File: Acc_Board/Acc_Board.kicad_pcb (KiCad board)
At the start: 2 copper layers, 139.7 x 88.9 mm, 84 parts, among them J1 AIRs Power, J10 Conn_01x02_Pin, J12 776087-1, J2 IsoSPI, J3 IMD BAT, J4 HV Power, J5 HVIL, J6 IMD, J7 Current Sensor, J8 Fans, J9 Shutdown IL, K1 Relay_SPST-NO, K2 Latching Relay, Q1 STS6NF20V, Q2 STS6NF20V, Q3 STS6NF20V, Q4 STS6NF20V, U1 ISO1050DUB, U10 DK1A1B-12V, U11 NSL-32, U12 LTC6820, U13 NAND, U15 MCP6004, U16 NSL-32, U17 NSL-32, U2 NUCLEO-L432KC, U3 LM555N, U4 PQDE6W-Q110-S5-H-D, U5 R-78B5.0-2.0, U6 NSL-32, U7 DK1A1B-12V, U8 LM7809_TO220, U9 NSL-32

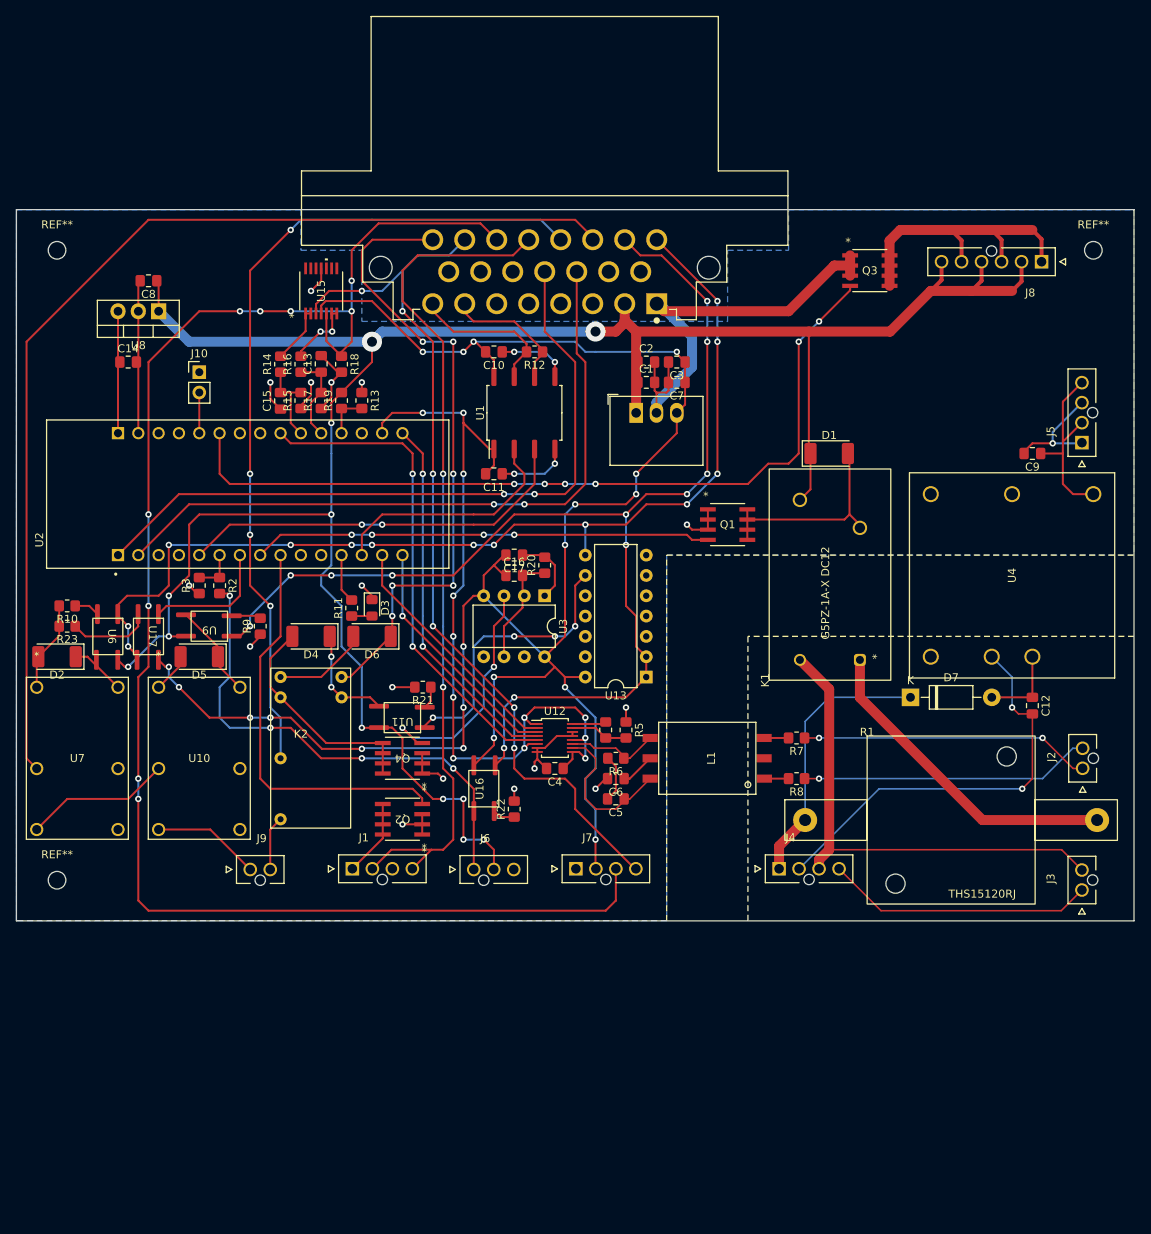
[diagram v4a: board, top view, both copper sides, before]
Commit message: acc board silkscreen done
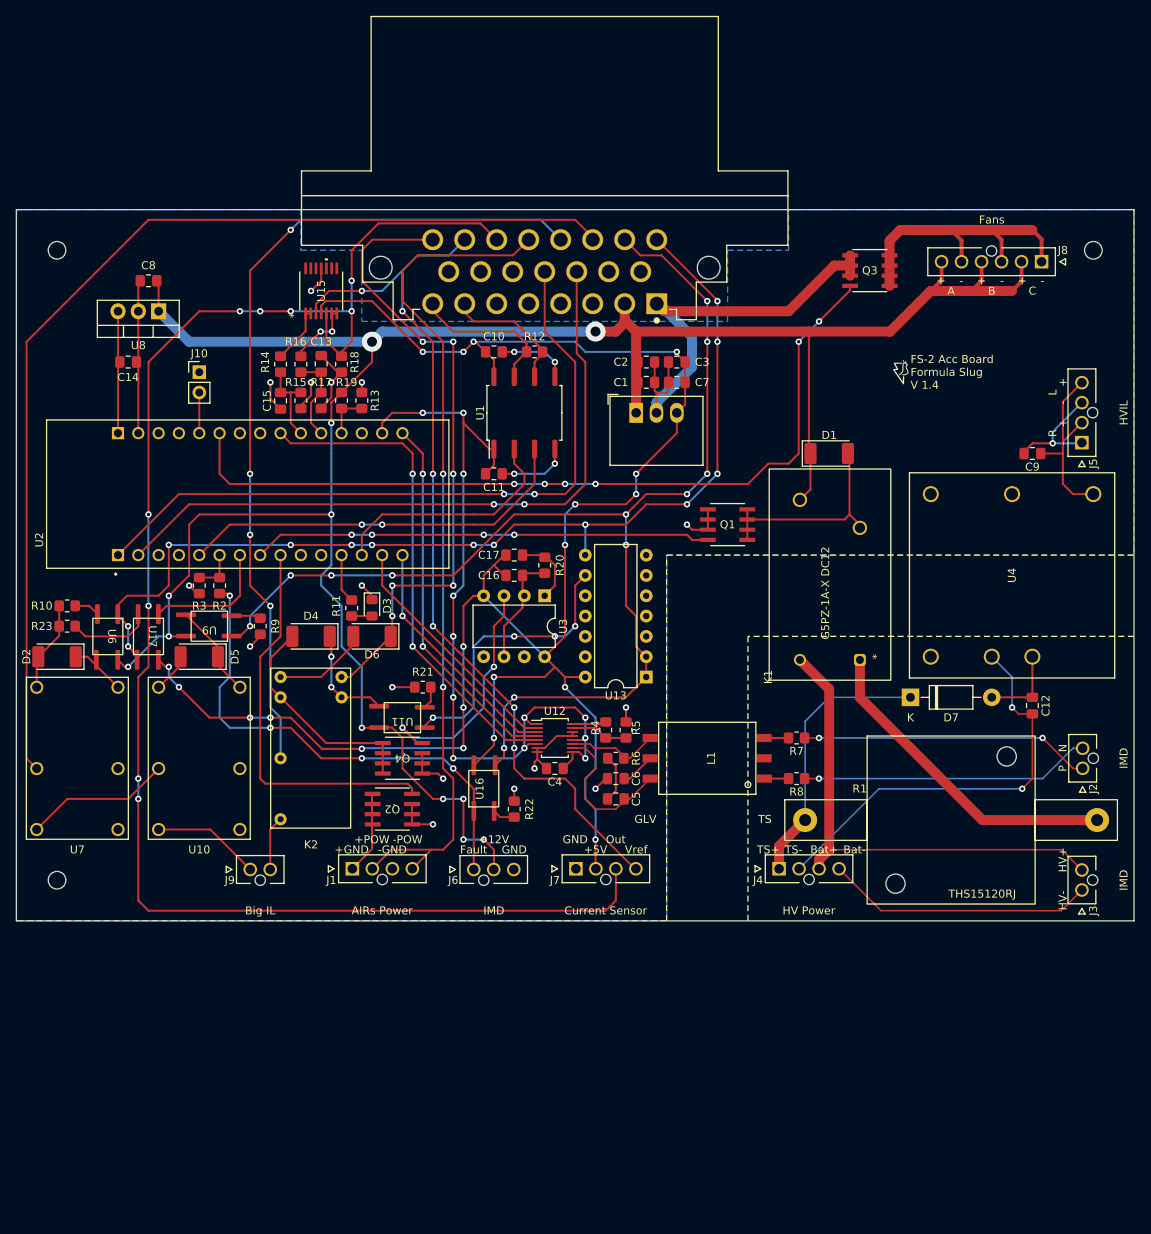
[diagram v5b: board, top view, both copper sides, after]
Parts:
- added G***: LOGO, 1FS_2_Global_Footprint_Library:FORMULA SLUG, F.Cu at (126.4, 33.1)
- moved Q2 1.80 mm to (59.7, 87.6)
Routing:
- net /Precharge_Control: track 51.0 -> 49.2 mm
- net /AIRS+_GND: track 9.67 -> 10.5 mm
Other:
- board text added: "+"
- board text added: "+12V"
- board text added: "+5V"
- board text added: "+GND"
- board text added: "+POW"
- board text added: "-"
- board text added: "-GND"
- board text added: "-POW"
- board text added: "A"
- board text added: "AIRs Power"
- board text added: "B"
- board text added: "Bat+"
- board text added: "Bat-"
- board text added: "Big IL"
- board text added: "C"
- board text added: "Current Sensor"
- board text added: "FS-2 Acc Board Formula Slug V 1.4"
- board text added: "Fans"
- board text added: "Fault"
- board text added: "GLV"
- board text added: "GND"
- board text added: "HV Power"
- board text added: "HV+"
- board text added: "HV-"
- board text added: "HVIL"
- board text added: "IMD"
- board text added: "L"
- board text added: "N"
- board text added: "Out"
- board text added: "P"
- board text added: "R"
- board text added: "TS"
- board text added: "TS+"
- board text added: "TS-"
- board text added: "Vref"

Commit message: Fixed sharp angle traces on acc board
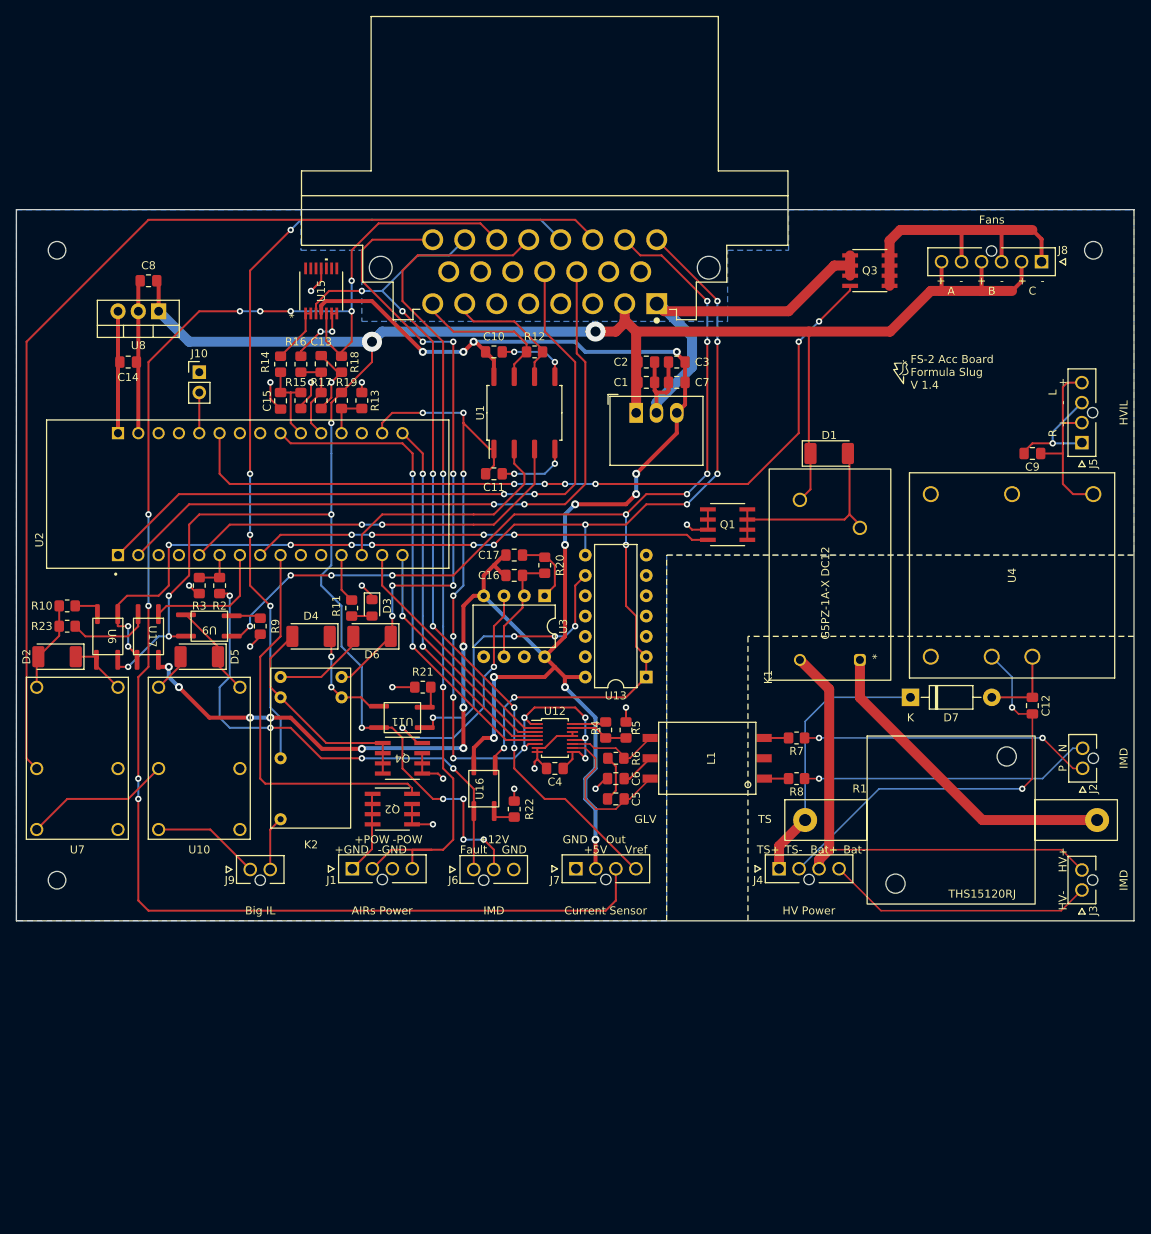
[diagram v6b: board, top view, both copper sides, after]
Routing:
- net /Current_Vref: track 113.0 -> 110.0 mm
- net /BMS_FAULT_5V: track 128.0 -> 129.5 mm
- net /Fan_Control: track 103.2 -> 101.7 mm
- net +12V: track 289.9 -> 288.5 mm
- net /AIRS+_12V: track 106.1 -> 107.5 mm
- net +5V: track 240.9 -> 242.2 mm
- net Net-(J8-Pad1): track 37.5 -> 36.5 mm
- net Net-(D2-K): track 6.87 -> 7.75 mm

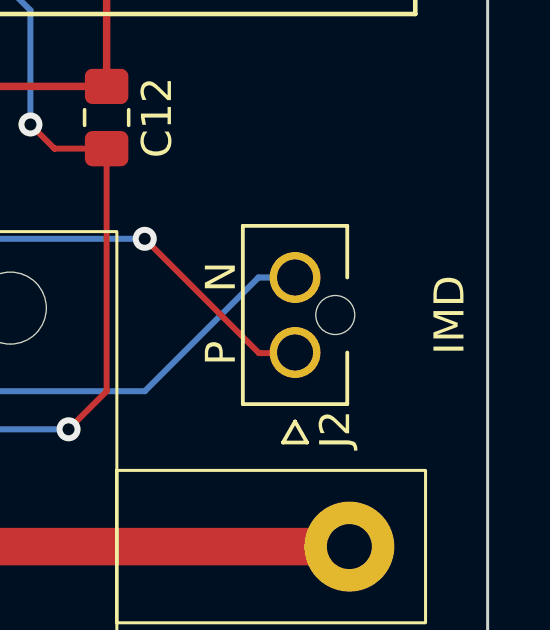
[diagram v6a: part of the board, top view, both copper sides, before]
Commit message: fixed minor silkscreen issue
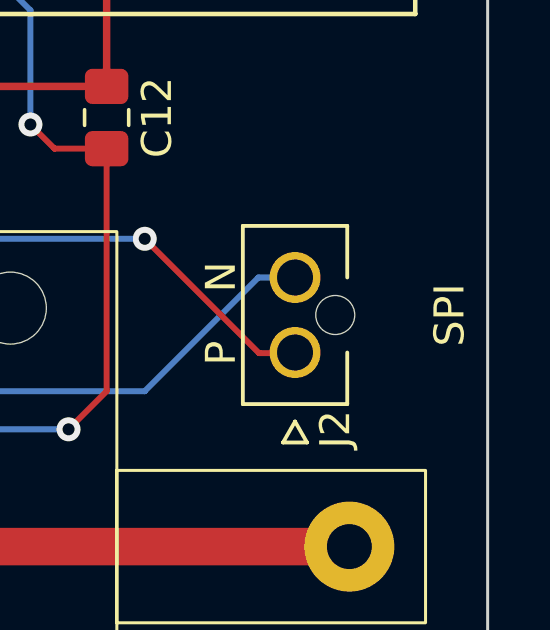
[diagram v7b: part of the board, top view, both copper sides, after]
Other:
- board text added: "SPI"
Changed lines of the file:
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@@
     (effects (font (size 1 1) (thickness 0.15)))
   )
-  (gr_text "IMD" (at 151.13 81.28 90) (layer "F.SilkS")
+  (gr_text "SPI" (at 151.13 81.28 90) (layer "F.SilkS")
     (effects (font (size 1 1) (thickness 0.15)))
   )

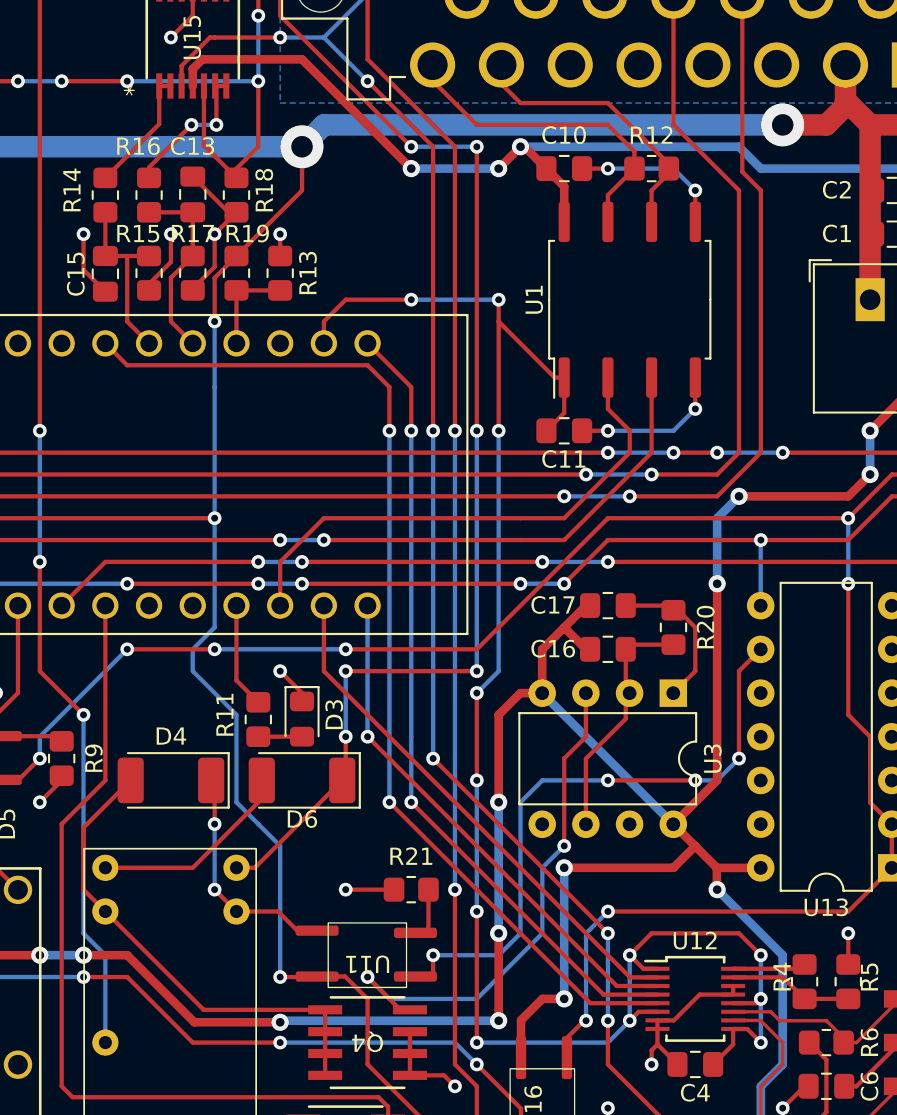
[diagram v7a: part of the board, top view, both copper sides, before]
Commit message: acc board minor fixes to trace isolation
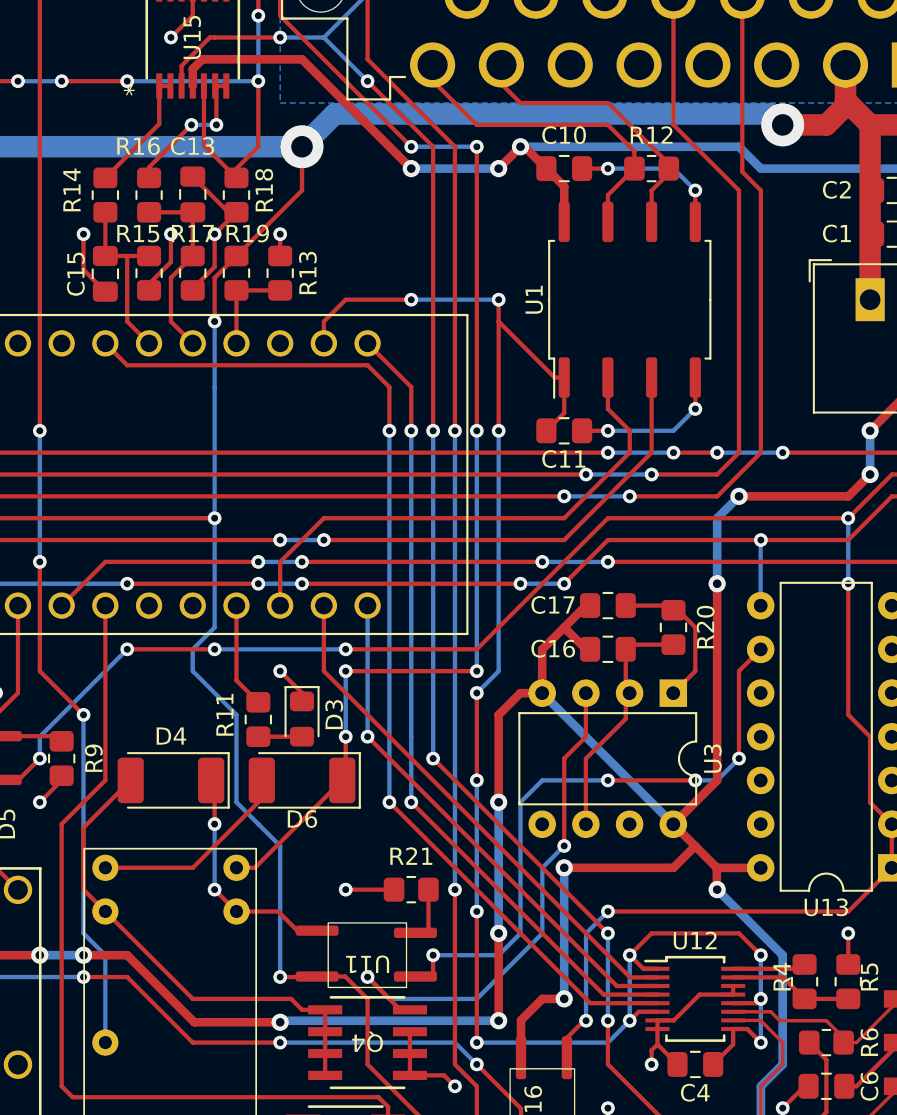
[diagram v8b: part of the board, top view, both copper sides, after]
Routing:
- net +12V: track 288.5 -> 289.0 mm
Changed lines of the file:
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@@
   (via (at 68.58 91.44) (size 0.8) (drill 0.4) (layers "F.Cu" "B.Cu") (net 1))
   (via (at 55.88 77.47) (size 0.8) (drill 0.4) (layers "F.Cu" "B.Cu") (net 1))
-  (segment (start 58.42 27.94) (end 57.15 29.21) (width 1.25) (layer "B.Cu") (net 1))
+  (segment (start 84.455 27.305) (end 59.055 27.305) (width 1.25) (layer "B.Cu") (net 1))
   (segment (start 50.8 59.69) (end 53.34 62.23) (width 0.25) (layer "B.Cu") (net 1))
   (segment (start 53.34 62.23) (end 53.34 67.31) (width 0.25) (layer "B.Cu") (net 1))
@@
   (segment (start 50.8 58.42) (end 50.8 59.69) (width 0.25) (layer "B.Cu") (net 1))
   (segment (start 52.07 43.18) (end 52.07 50.8) (width 0.25) (layer "B.Cu") (net 1))
+  (segment (start 85.09 27.94) (end 84.455 27.305) (width 1.25) (layer "B.Cu") (net 1))
   (segment (start 52.07 39.37) (end 52.07 41.91) (width 0.25) (layer "B.Cu") (net 1))
+  (segment (start 59.055 27.305) (end 57.15 29.21) (width 1.25) (layer "B.Cu") (net 1))
   (segment (start 68.58 86.36) (end 66.04 86.36) (width 0.25) (layer "B.Cu") (net 1))
   (segment (start 52.07 50.8) (end 52.07 57.15) (width 0.25) (layer "B.Cu") (net 1))
@@
   (segment (start 31.75 66.04) (end 30.48 66.04) (width 0.25) (layer "B.Cu") (net 1))
   (segment (start 30.48 66.04) (end 26.67 69.85) (width 0.25) (layer "B.Cu") (net 1))
-  (segment (start 85.09 27.94) (end 58.42 27.94) (width 1.25) (layer "B.Cu") (net 1))
   (segment (start 52.07 41.91) (end 52.07 43.18) (width 0.25) (layer "B.Cu") (net 1))
   (segment (start 138.6625 42.9475) (end 138.6625 43.18) (width 0.25) (layer "F.Cu") (net 2))
@@
   (via (at 52.07 68.58) (size 0.8) (drill 0.4) (layers "F.Cu" "B.Cu") (net 14))
   (segment (start 52.07 72.39) (end 52.07 68.58) (width 0.25) (layer "B.Cu") (net 14))
-  (segment (start 51.435 79.375) (end 45.72 73.66) (width 0.25) (layer "F.Cu") (net 15))
-  (segment (start 58.4962 79.375) (end 51.435 79.375) (width 0.25) (layer "F.Cu") (net 15))
+  (segment (start 58.4962 79.375) (end 57.15 79.375) (width 0.25) (layer "F.Cu") (net 15))
+  (segment (start 57.15 79.375) (end 56.515 78.74) (width 0.25) (layer "F.Cu") (net 15))
   (segment (start 44.45 68.7825) (end 44.45 72.39) (width 0.25) (layer "F.Cu") (net 15))
   (segment (start 47.1925 66.04) (end 44.45 68.7825) (width 0.25) (layer "F.Cu") (net 15))
+  (segment (start 50.8 78.74) (end 45.72 73.66) (width 0.25) (layer "F.Cu") (net 15))
   (segment (start 44.45 72.39) (end 45.72 73.66) (width 0.25) (layer "F.Cu") (net 15))
   (segment (start 58.4962 83.185) (end 58.4962 79.375) (width 0.25) (layer "F.Cu") (net 15))
+  (segment (start 56.515 78.74) (end 50.8 78.74) (width 0.25) (layer "F.Cu") (net 15))
   (segment (start 33.898 63.343) (end 37.8975 67.3425) (width 0.25) (layer "F.Cu") (net 16))
   (segment (start 40.64 72.4027) (end 37.8975 69.6602) (width 0.25) (layer "F.Cu") (net 16))
